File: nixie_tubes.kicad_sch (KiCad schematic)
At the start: 12 parts

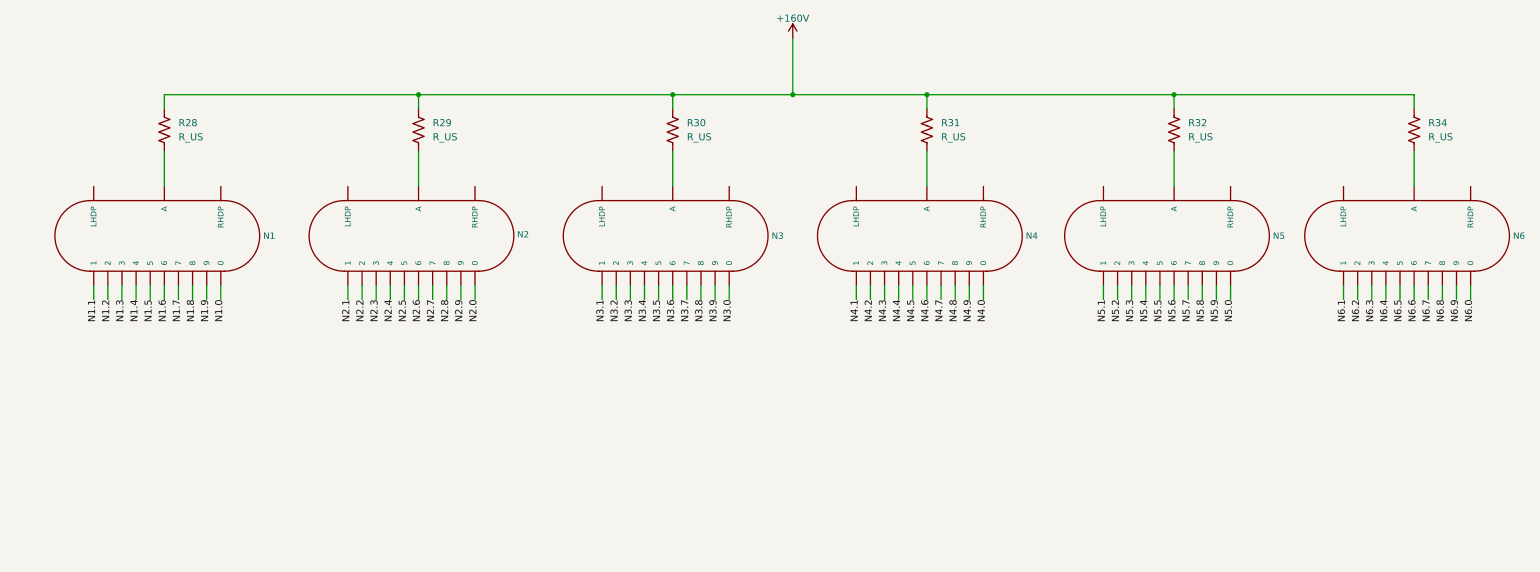
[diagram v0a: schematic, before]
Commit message: Update power supply layout and add associated components
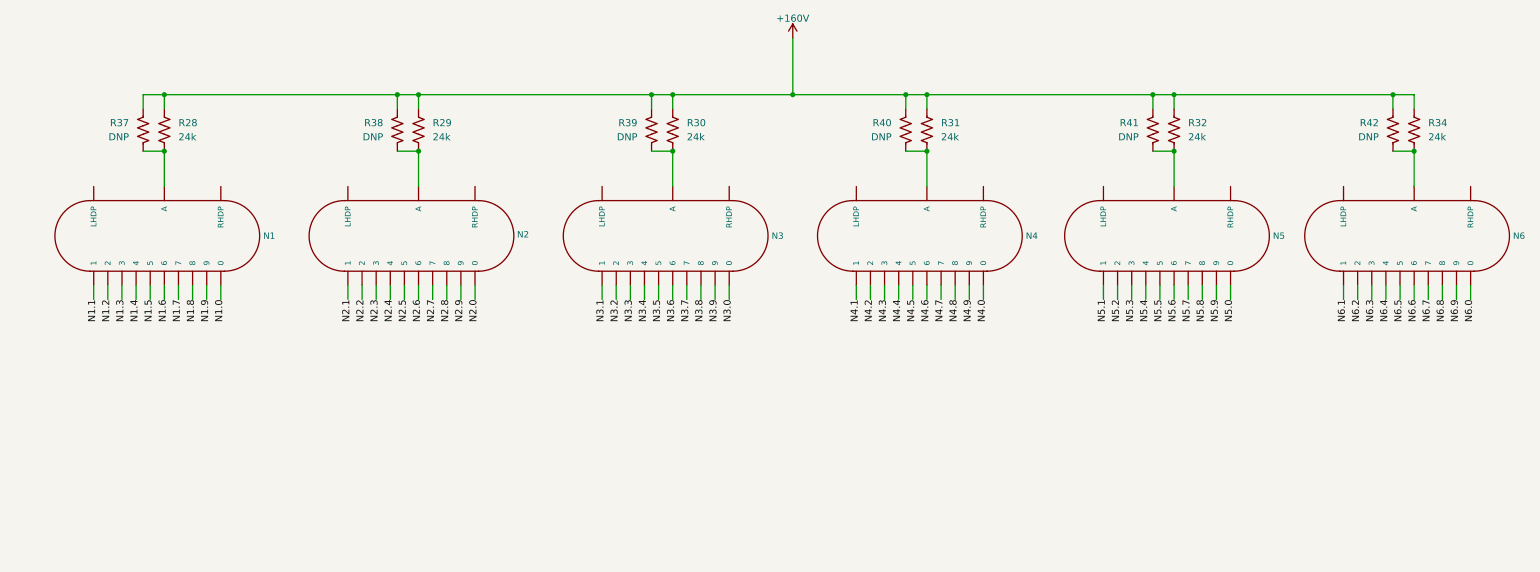
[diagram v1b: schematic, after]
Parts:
- added R37, R38, R39, R40, R41, R42: DNP, Resistor_THT:R_Axial_DIN0207_L6.3mm_D2.5mm_P10.16mm_Horizontal, symbol Device:R_US
- R28, R29, R30, R31, R32, R34: value R_US -> 24k; footprint (none) -> Resistor_SMD:R_2512_6332Metric
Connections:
- net +160V: now also R37.1, R38.1, R39.1, R40.1, R41.1, R42.1
- net at N3.A, R30.2: now also R39.2
- net at N1.A, R28.2: now also R37.2
- net at N4.A, R31.2: now also R40.2
- net at N5.A, R32.2: now also R41.2
- net at N2.A, R29.2: now also R38.2
- net at N6.A, R34.2: now also R42.2

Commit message: Add backlight LEDs
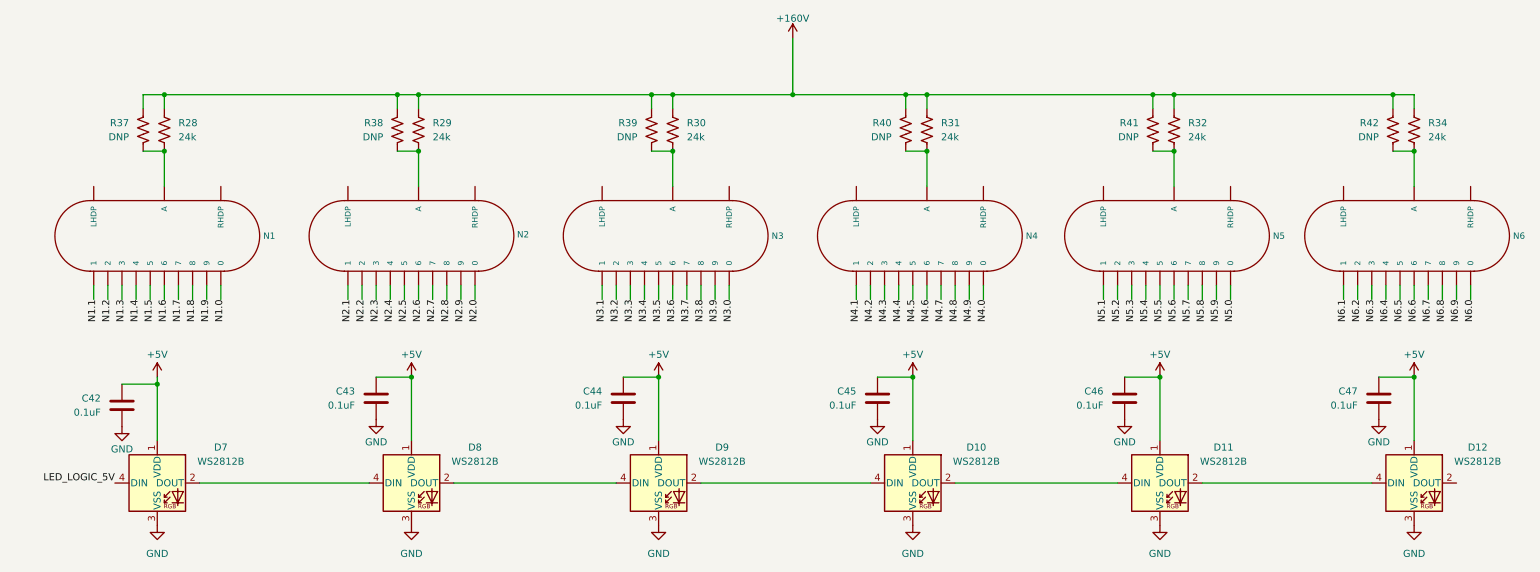
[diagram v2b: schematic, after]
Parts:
- added C42, C43, C44, C45, C46, C47: 0.1uF, Capacitor_SMD:C_0603_1608Metric, symbol Device:C
- added D10, D11, D12, D7, D8, D9: WS2812B, LED_SMD:LED_WS2812B_PLCC4_5.0x5.0mm_P3.2mm, symbol LED:WS2812B
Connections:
- new net: D8.2 (DOUT), D9.4 (DIN)
- new net: D7.2 (DOUT), D8.4 (DIN)
- new net: D11.2 (DOUT), D12.4 (DIN)
- new net: D10.2 (DOUT), D11.4 (DIN)
- new net: D10.4 (DIN), D9.2 (DOUT)
- new net +5V: C42.1, C43.1, C44.1, C45.1, C46.1, C47.1, D10.1 (VDD), D11.1 (VDD), D12.1 (VDD), D7.1 (VDD), D8.1 (VDD), D9.1 (VDD)
- new net GND: C42.2, C43.2, C44.2, C45.2, C46.2, C47.2, D10.3 (VSS), D11.3 (VSS), D12.3 (VSS), D7.3 (VSS), D8.3 (VSS), D9.3 (VSS)
- new net LED_LOGIC_5V: D7.4 (DIN)

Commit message: Add power supply footprints; begin layout
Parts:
- N1, N2, N3, N4, N5, N6: footprint nixies-us_IN-14 -> eclectronics_nixie_footprints:nixies-us-IN-14
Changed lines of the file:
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@@
 			)
 		)
-		(property "Footprint" "nixies-us_IN-14"
+		(property "Footprint" "eclectronics_nixie_footprints:nixies-us-IN-14"
 			(at 121.92 79.248 0)
 			(effects
@@
 			)
 		)
-		(property "Footprint" "nixies-us_IN-14"
+		(property "Footprint" "eclectronics_nixie_footprints:nixies-us-IN-14"
 			(at 255.27 79.248 0)
 			(effects
@@
 			)
 		)
-		(property "Footprint" "nixies-us_IN-14"
+		(property "Footprint" "eclectronics_nixie_footprints:nixies-us-IN-14"
 			(at 212.09 79.248 0)
 			(effects
@@
 			)
 		)
-		(property "Footprint" "nixies-us_IN-14"
+		(property "Footprint" "eclectronics_nixie_footprints:nixies-us-IN-14"
 			(at 167.64 79.248 0)
 			(effects
@@
 			)
 		)
-		(property "Footprint" "nixies-us_IN-14"
+		(property "Footprint" "eclectronics_nixie_footprints:nixies-us-IN-14"
 			(at 76.2 79.248 0)
 			(effects
@@
 			)
 		)
-		(property "Footprint" "nixies-us_IN-14"
+		(property "Footprint" "eclectronics_nixie_footprints:nixies-us-IN-14"
 			(at 30.48 79.248 0)
 			(effects

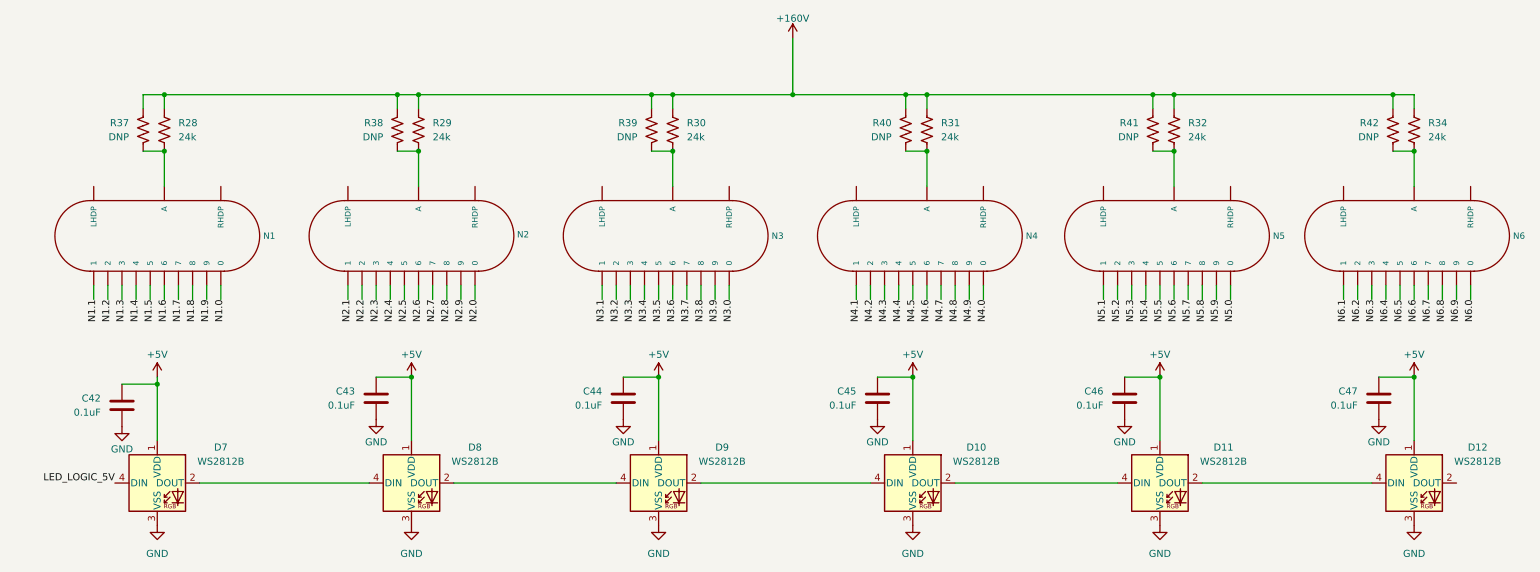
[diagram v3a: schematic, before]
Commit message: Add global labels for nets spanning several sheets
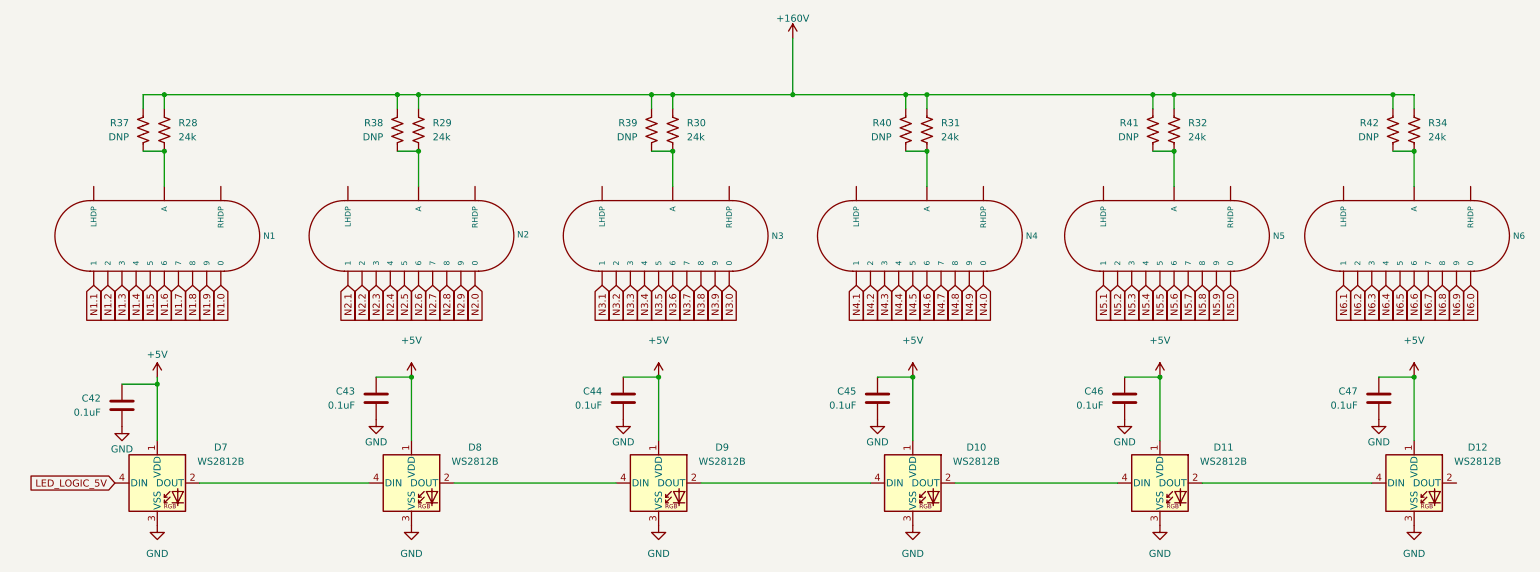
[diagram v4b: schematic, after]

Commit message: Add DigiKey part numbers to components
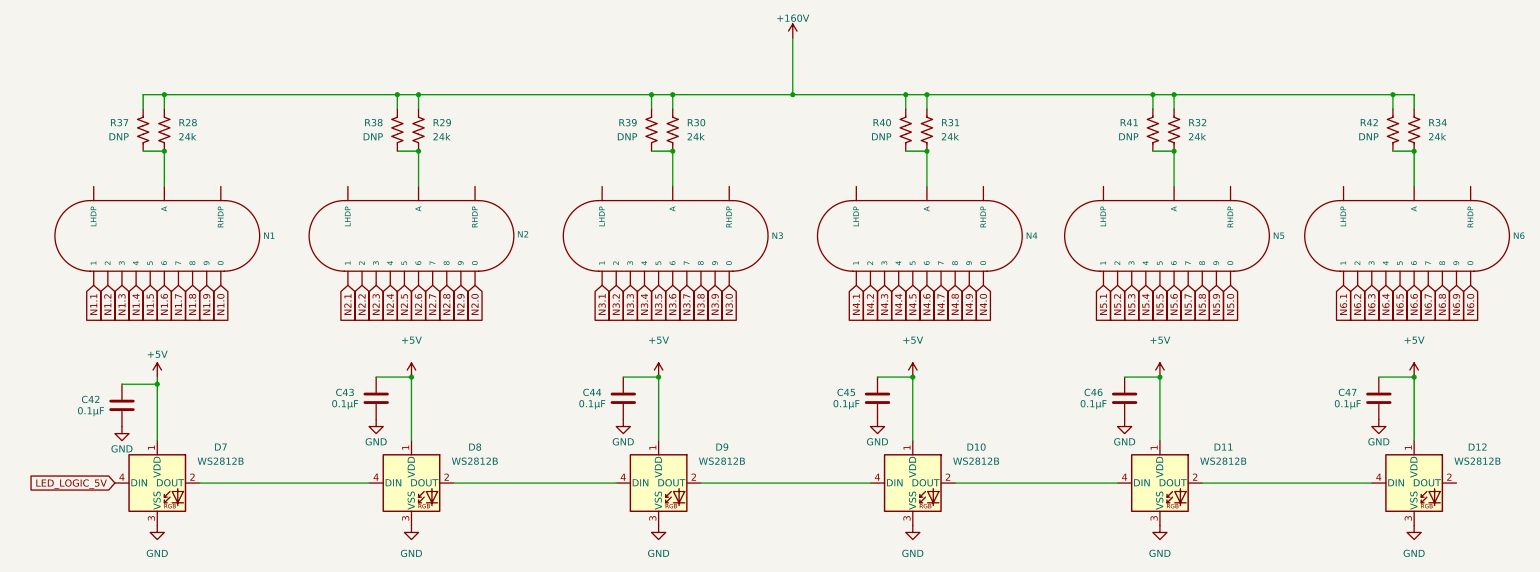
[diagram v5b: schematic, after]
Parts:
- C42, C43, C44, C45, C46, C47: value 0.1uF -> 0.1µF; DigikeyPN (none) -> 1276-1033-1-ND
- D10, D11, D12, D7, D8, D9: DigikeyPN (none) -> 1568-16347CT-ND
- R28, R29, R30, R31, R32, R34: DigikeyPN (none) -> RMCF2512JT24K0CT-ND
